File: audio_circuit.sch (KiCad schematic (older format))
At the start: 23 parts

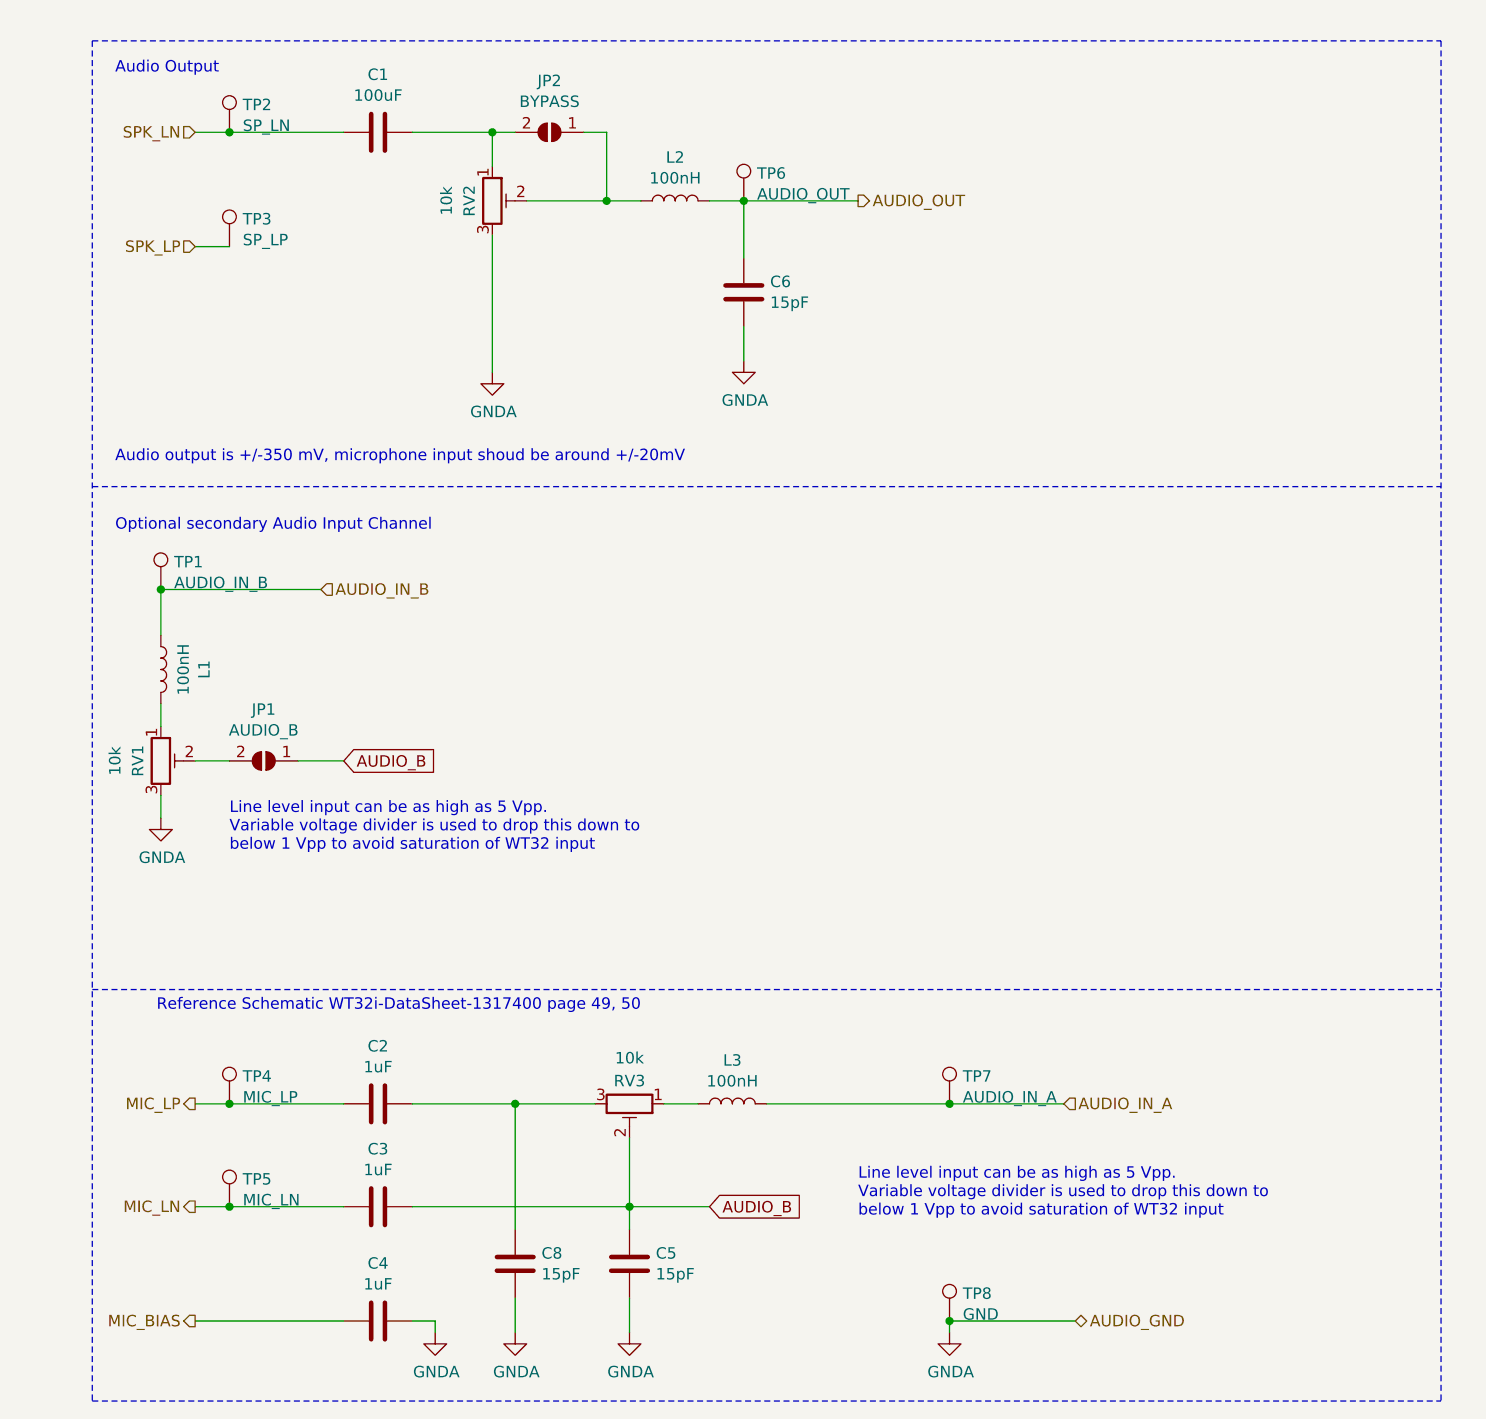
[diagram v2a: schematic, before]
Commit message: [#1] Reworked audio path
* Swaped LN and LP for better reading
* Rearanged audio-in cirquid
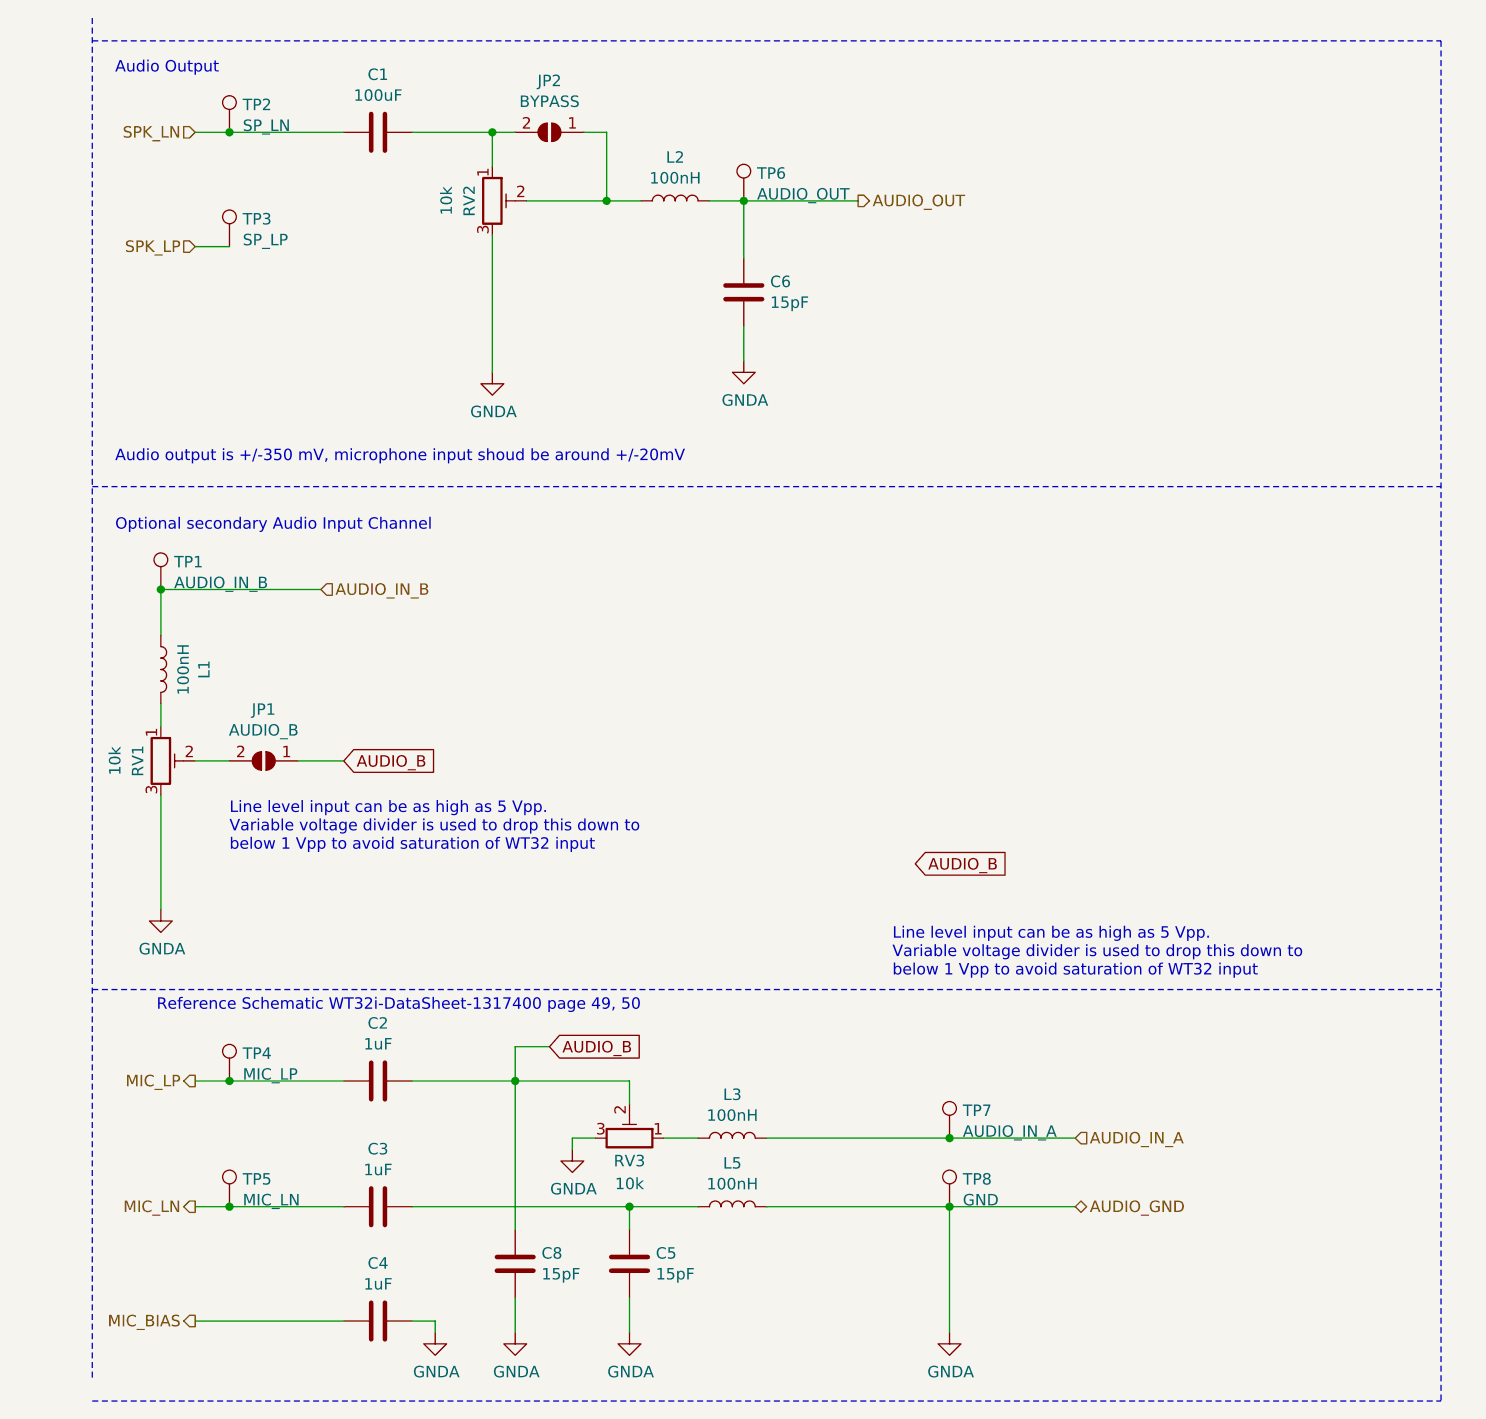
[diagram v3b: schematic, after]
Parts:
- added L5: 100nH, Inductor_SMD:L_0805_2012Metric_Pad1.15x1.40mm_HandSolder, symbol Device:L
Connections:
- net AUDIO_B: now also C2.1, C8.1; no longer C3.1, C5.1
- net GNDA: now also RV3.3, L5.2
- new net: C3.1, C5.1, L5.1
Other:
- moved on the sheet: C2, L3, RV3, TP4, TP7, TP8
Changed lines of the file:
@@
 Comment4 "Author:"
 $EndDescr
-Text HLabel 1250 5900 0    50   Output ~ 0
-MIC_LP
-Text HLabel 1250 6350 0    50   Output ~ 0
-MIC_LN
 Text HLabel 1250 1650 0    50   Input ~ 0
 SPK_LN
 Text HLabel 4150 1950 2    50   Output ~ 0
 AUDIO_OUT
-Text HLabel 5050 5900 2    50   Input ~ 0
+Text HLabel 5100 6050 2    50   Input ~ 0
 AUDIO_IN_A
-Text HLabel 5100 6850 2    50   BiDi ~ 0
+Text HLabel 5100 6350 2    50   BiDi ~ 0
 AUDIO_GND
 Text HLabel 1250 6850 0    50   Output ~ 0
@@
 L power:GNDA #PWR018
 U 1 1 5C1B2321
-P 3150 6900
-F 0 "#PWR018" H 3150 6650 50  0001 C CNN
-F 1 "GNDA" H 3155 6727 50  0000 C CNN
-F 2 "" H 3150 6900 50  0001 C CNN
-F 3 "" H 3150 6900 50  0001 C CNN
-	1    3150 6900
-	1    0    0    -1
-$EndComp
-Text Notes 4150 6400 0    50   ~ 0
+P 2900 6100
+F 0 "#PWR018" H 2900 5850 50  0001 C CNN
+F 1 "GNDA" H 2905 5927 50  0000 C CNN
+F 2 "" H 2900 6100 50  0001 C CNN
+F 3 "" H 2900 6100 50  0001 C CNN
+	1    2900 6100
+	1    0    0    -1
+$EndComp
+Text Notes 4300 5350 0    50   ~ 0
 Line level input can be as high as 5 Vpp.\nVariable voltage divider is used to drop this down to\nbelow 1 Vpp to avoid saturation of WT32 input
 Text Notes 900  3400 0    50   ~ 0
@@
 	1    0    0    -1
 $EndComp
-Wire Wire Line
-	4550 6900 4550 6850
 $Comp
 L Device:L L3
 U 1 1 5BFC0C35
-P 3600 5900
-F 0 "L3" V 3790 5900 50  0000 C CNN
-F 1 "100nH" V 3699 5900 50  0000 C CNN
-F 2 "Inductor_SMD:L_0805_2012Metric_Pad1.15x1.40mm_HandSolder" H 3600 5900 50  0001 C CNN
-F 3 "~" H 3600 5900 50  0001 C CNN
-F 4 "810-MLF2012DR10MT000" H 300 -100 50  0001 C CNN "Mouser Best.Nr."
-	1    3600 5900
+P 3600 6050
+F 0 "L3" V 3790 6050 50  0000 C CNN
+F 1 "100nH" V 3699 6050 50  0000 C CNN
+F 2 "Inductor_SMD:L_0805_2012Metric_Pad1.15x1.40mm_HandSolder" H 3600 6050 50  0001 C CNN
+F 3 "~" H 3600 6050 50  0001 C CNN
+F 4 "810-MLF2012DR10MT000" H 300 50  50  0001 C CNN "Mouser Best.Nr."
+	1    3600 6050
 	0    -1   -1   0
 $EndComp
 Wire Notes Line
-	800  1250 800  7200
+	800  1150 800  7100
 Text HLabel 1800 3650 2    50   Input ~ 0
 AUDIO_IN_B
@@
 Wire Notes Line
 	800  3200 6700 3200
-$Comp
-L Connector:TestPoint TP8
-U 1 1 5C0DF1AC
-P 4550 6850
-F 0 "TP8" H 4608 6970 50  0000 L CNN
-F 1 "GND" H 4608 6879 50  0000 L CNN
-F 2 "TestPoint:TestPoint_Pad_4.0x4.0mm" H 4750 6850 50  0001 C CNN
-F 3 "~" H 4750 6850 50  0001 C CNN
-F 4 "-" H 0   0   50  0001 C CNN "Mouser Best.Nr."
-	1    4550 6850
-	1    0    0    -1
-$EndComp
-Connection ~ 4550 6850
-Wire Wire Line
-	3300 5900 3450 5900
+Connection ~ 4550 6350
 $Comp
 L Device:R_POT_TRIM RV3
 U 1 1 5BFC4F3F
-P 3150 5900
-F 0 "RV3" V 3050 5900 50  0000 C CNN
-F 1 "10k" V 2950 5900 50  0000 C CNN
-F 2 "Potentiometer_SMD:Potentiometer_Vishay_TS53YL_Vertical" H 3150 5900 50  0001 C CNN
-F 3 "~" H 3150 5900 50  0001 C CNN
-F 4 " 72-TS53YL-10K" H 300 -100 50  0001 C CNN "Mouser Best.Nr."
-	1    3150 5900
-	0    1    1    0
+P 3150 6050
+F 0 "RV3" V 3050 6050 50  0000 C CNN
+F 1 "10k" V 2950 6050 50  0000 C CNN
+F 2 "Potentiometer_SMD:Potentiometer_Vishay_TS53YL_Vertical" H 3150 6050 50  0001 C CNN
+F 3 "~" H 3150 6050 50  0001 C CNN
+F 4 " 72-TS53YL-10K" H 300 50  50  0001 C CNN "Mouser Best.Nr."
+	1    3150 6050
+	0    1    -1   0
 $EndComp
 $Comp
@@
 L Device:C C2
 U 1 1 5BFC0997
-P 2050 5900
-F 0 "C2" V 1798 5900 50  0000 C CNN
-F 1 "1uF" V 1889 5900 50  0000 C CNN
-F 2 "Capacitor_SMD:C_0805_2012Metric_Pad1.15x1.40mm_HandSolder" H 2088 5750 50  0001 C CNN
-F 3 "~" H 2050 5900 50  0001 C CNN
-F 4 "TBD" H 150 -100 50  0001 C CNN "Mouser Best.Nr."
-F 5 "Tantal neccessary?" H 2050 5900 50  0001 C CNN "Notes"
-	1    2050 5900
+P 2050 5800
+F 0 "C2" V 1798 5800 50  0000 C CNN
+F 1 "1uF" V 1889 5800 50  0000 C CNN
+F 2 "Capacitor_SMD:C_0805_2012Metric_Pad1.15x1.40mm_HandSolder" H 2088 5650 50  0001 C CNN
+F 3 "~" H 2050 5800 50  0001 C CNN
+F 4 "TBD" H 150 -200 50  0001 C CNN "Mouser Best.Nr."
+F 5 "Tantal neccessary?" H 2050 5800 50  0001 C CNN "Notes"
+	1    2050 5800
 	0    1    1    0
 $EndComp
@@
 	1    0    0    -1
 $EndComp
-Connection ~ 3150 6350
-Wire Wire Line
-	3150 6350 3150 6450
 Wire Wire Line
 	3150 6750 3150 6900
@@
 L power:GNDA #PWR014
 U 1 1 5C7723EC
-P 1100 4650
-F 0 "#PWR014" H 1100 4400 50  0001 C CNN
-F 1 "GNDA" H 1105 4477 50  0000 C CNN
-F 2 "" H 1100 4650 50  0001 C CNN
-F 3 "" H 1100 4650 50  0001 C CNN
-	1    1100 4650
-	1    0    0    -1
-$EndComp
-Wire Wire Line
-	4550 6850 5100 6850
+P 1100 5050
+F 0 "#PWR014" H 1100 4800 50  0001 C CNN
+F 1 "GNDA" H 1105 4877 50  0000 C CNN
+F 2 "" H 1100 5050 50  0001 C CNN
+F 3 "" H 1100 5050 50  0001 C CNN
+	1    1100 5050
+	1    0    0    -1
+$EndComp
+Wire Wire Line
+	4550 6350 5100 6350
 $Comp
 L Jumper:SolderJumper_2_Open JP1
@@
 	1100 4150 1100 4250
 Wire Wire Line
-	1100 4550 1100 4650
-Wire Wire Line
 	1250 4400 1400 4400
 Text GLabel 1900 4400 2    50   Input ~ 0
@@
 Wire Wire Line
 	1700 4400 1900 4400
-Wire Wire Line
-	3150 6350 3500 6350
-Text GLabel 3500 6350 2    50   Input ~ 0
+Text GLabel 4400 4850 2    50   Input ~ 0
 AUDIO_B
 Text Notes 1400 4800 0    50   ~ 0
@@
 Wire Wire Line
 	2550 2100 2550 2700
-Wire Wire Line
-	3150 6050 3150 6350
 $Comp
 L Connector:TestPoint TP7
 U 1 1 5C7783F5
-P 4550 5900
-F 0 "TP7" H 4608 6020 50  0000 L CNN
-F 1 "AUDIO_IN_A" H 4608 5929 50  0000 L CNN
-F 2 "TestPoint:TestPoint_Pad_D1.5mm" H 4750 5900 50  0001 C CNN
-F 3 "~" H 4750 5900 50  0001 C CNN
-F 4 "-" H 0   0   50  0001 C CNN "Mouser Best.Nr."
-	1    4550 5900
-	1    0    0    -1
-$EndComp
-Wire Wire Line
-	4550 5900 5050 5900
-Wire Wire Line
-	4550 5900 3750 5900
-Connection ~ 4550 5900
-Wire Wire Line
-	1250 5900 1400 5900
+P 4550 6050
+F 0 "TP7" H 4608 6170 50  0000 L CNN
+F 1 "AUDIO_IN_A" H 4608 6079 50  0000 L CNN
+F 2 "TestPoint:TestPoint_Pad_D1.5mm" H 4750 6050 50  0001 C CNN
+F 3 "~" H 4750 6050 50  0001 C CNN
+F 4 "-" H 0   150 50  0001 C CNN "Mouser Best.Nr."
+	1    4550 6050
+	1    0    0    -1
+$EndComp
+Wire Wire Line
+	4550 6050 3750 6050
+Connection ~ 4550 6050
+Wire Wire Line
+	1250 5800 1400 5800
 Wire Wire Line
 	1250 6350 1400 6350
 Wire Wire Line
 	1250 6850 1900 6850
-$Comp
-L Connector:TestPoint TP4
-U 1 1 5C77A38C
-P 1400 5900
-F 0 "TP4" H 1458 6020 50  0000 L CNN
-F 1 "MIC_LP" H 1458 5929 50  0000 L CNN
-F 2 "TestPoint:TestPoint_Pad_D1.5mm" H 1600 5900 50  0001 C CNN
-F 3 "~" H 1600 5900 50  0001 C CNN
-F 4 "-" H 0   0   50  0001 C CNN "Mouser Best.Nr."
-	1    1400 5900
-	1    0    0    -1
-$EndComp
-Connection ~ 1400 5900
-Wire Wire Line
-	1400 5900 1900 5900
+Connection ~ 1400 5800
+Wire Wire Line
+	1400 5800 1900 5800
 $Comp
 L Connector:TestPoint TP5
@@
 Wire Wire Line
 	2650 6750 2650 6900
-Wire Wire Line
-	2200 5900 2650 5900
+$Comp
+L Connector:TestPoint TP4
+U 1 1 5C77A38C
+P 1400 5800
+F 0 "TP4" H 1458 5920 50  0000 L CNN
+F 1 "MIC_LP" H 1458 5829 50  0000 L CNN
+F 2 "TestPoint:TestPoint_Pad_D1.5mm" H 1600 5800 50  0001 C CNN
+F 3 "~" H 1600 5800 50  0001 C CNN
+F 4 "-" H 0   -100 50  0001 C CNN "Mouser Best.Nr."
+	1    1400 5800
+	1    0    0    -1
+$EndComp
+Text HLabel 1250 6350 0    50   Output ~ 0
+MIC_LN
+Text HLabel 1250 5800 0    50   Output ~ 0
+MIC_LP
+$Comp
+L Device:L L5
+U 1 1 5D4E74BE
+P 3600 6350
+F 0 "L5" V 3790 6350 50  0000 C CNN
+F 1 "100nH" V 3699 6350 50  0000 C CNN
+F 2 "Inductor_SMD:L_0805_2012Metric_Pad1.15x1.40mm_HandSolder" H 3600 6350 50  0001 C CNN
+F 3 "~" H 3600 6350 50  0001 C CNN
+F 4 "810-MLF2012DR10MT000" H 300 350 50  0001 C CNN "Mouser Best.Nr."
+	1    3600 6350
+	0    -1   -1   0
+$EndComp
+Wire Wire Line
+	3750 6350 4550 6350
+Wire Wire Line
+	2200 5800 2650 5800
+Wire Wire Line
+	3450 6050 3300 6050
+Wire Wire Line
+	3150 5800 3150 5900
 Wire Wire Line
 	2200 6350 3150 6350
 Wire Wire Line
-	2650 6450 2650 5900
-Connection ~ 2650 5900
-Wire Wire Line
-	2650 5900 3000 5900
+	3000 6050 2900 6050
+Wire Wire Line
+	2900 6050 2900 6100
+$Comp
+L Connector:TestPoint TP8
+U 1 1 5C0DF1AC
+P 4550 6350
+F 0 "TP8" H 4608 6470 50  0000 L CNN
+F 1 "GND" H 4608 6379 50  0000 L CNN
+F 2 "TestPoint:TestPoint_Pad_4.0x4.0mm" H 4750 6350 50  0001 C CNN
+F 3 "~" H 4750 6350 50  0001 C CNN
+F 4 "-" H 0   -500 50  0001 C CNN "Mouser Best.Nr."
+	1    4550 6350
+	1    0    0    -1
+$EndComp
+Wire Wire Line
+	4550 6350 4550 6900
+Wire Wire Line
+	4550 6050 5100 6050
+$Comp
+L power:GNDA #PWR039
+U 1 1 5D509442
+P 3150 6900
+F 0 "#PWR039" H 3150 6650 50  0001 C CNN
+F 1 "GNDA" H 3155 6727 50  0000 C CNN
+F 2 "" H 3150 6900 50  0001 C CNN
+F 3 "" H 3150 6900 50  0001 C CNN
+	1    3150 6900
+	1    0    0    -1
+$EndComp
+Wire Wire Line
+	3150 6450 3150 6350
+Connection ~ 3150 6350
+Wire Wire Line
+	3150 6350 3450 6350
+Connection ~ 2650 5800
+Wire Wire Line
+	2650 5800 3150 5800
+Wire Wire Line
+	1100 4550 1100 5050
+Text GLabel 2800 5650 2    50   Input ~ 0
+AUDIO_B
+Wire Wire Line
+	2650 6450 2650 5800
+Wire Wire Line
+	2650 5800 2650 5650
+Wire Wire Line
+	2650 5650 2800 5650
 $EndSCHEMATC

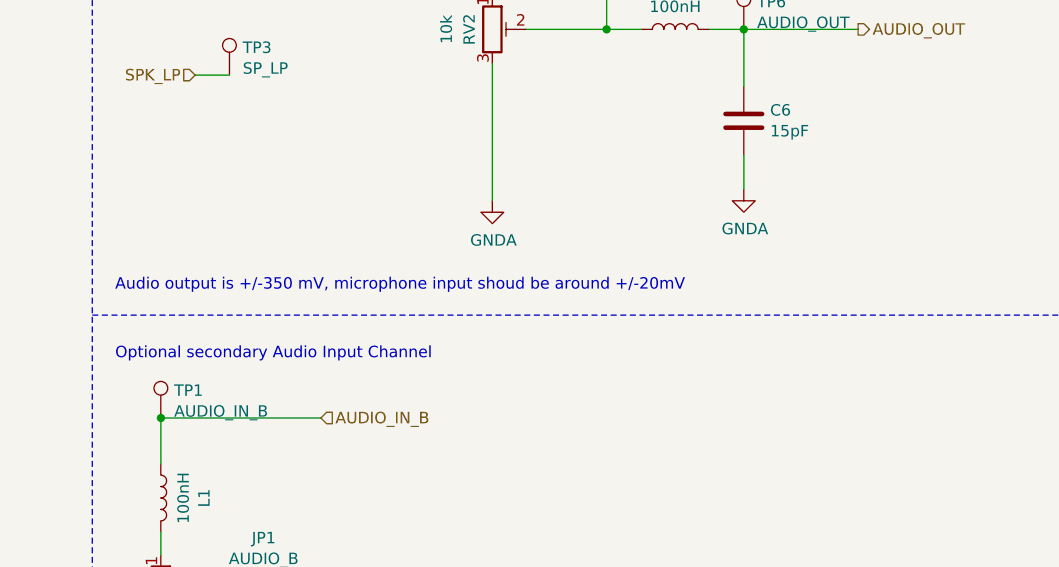
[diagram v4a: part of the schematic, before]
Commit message: Fix some comments
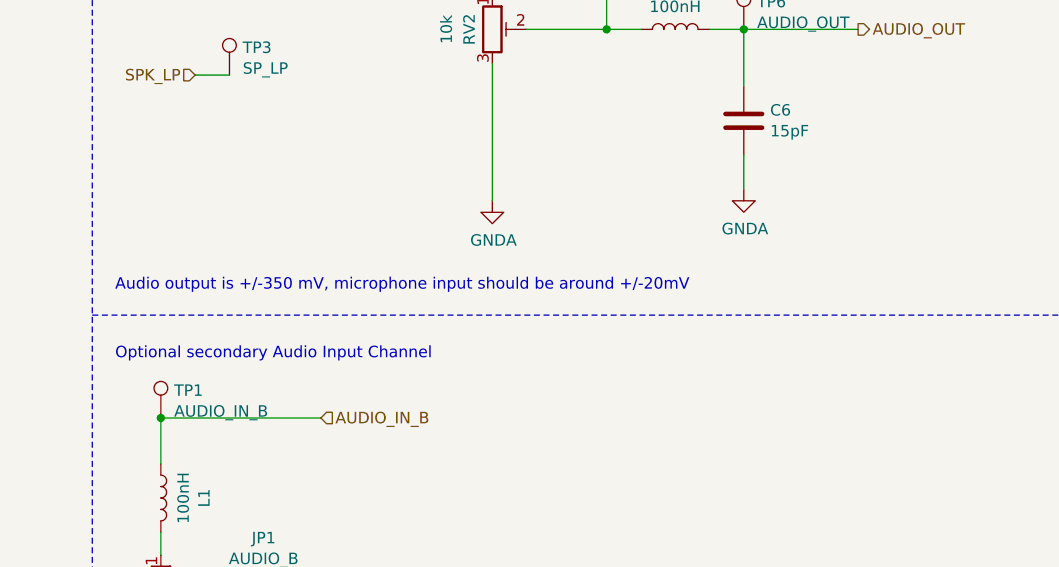
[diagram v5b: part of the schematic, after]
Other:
- note added: "Audio output is +/-350 mV, microphone input should be around +/-20mV"
- note removed: "Audio output is +/-350 mV, microphone input shoud be around +/-20mV"
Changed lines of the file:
@@
 EESchema Schematic File Version 4
 LIBS:bt-trx-dev-board-cache
-EELAYER 26 0
+EELAYER 29 0
 EELAYER END
 $Descr A4 11693 8268
@@
 	2550 1650 2550 1800
 Text Notes 900  3100 0    50   ~ 0
-Audio output is +/-350 mV, microphone input shoud be around +/-20mV
+Audio output is +/-350 mV, microphone input should be around +/-20mV
 Wire Wire Line
 	2550 2100 2550 2700
